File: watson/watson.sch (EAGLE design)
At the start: 37 parts

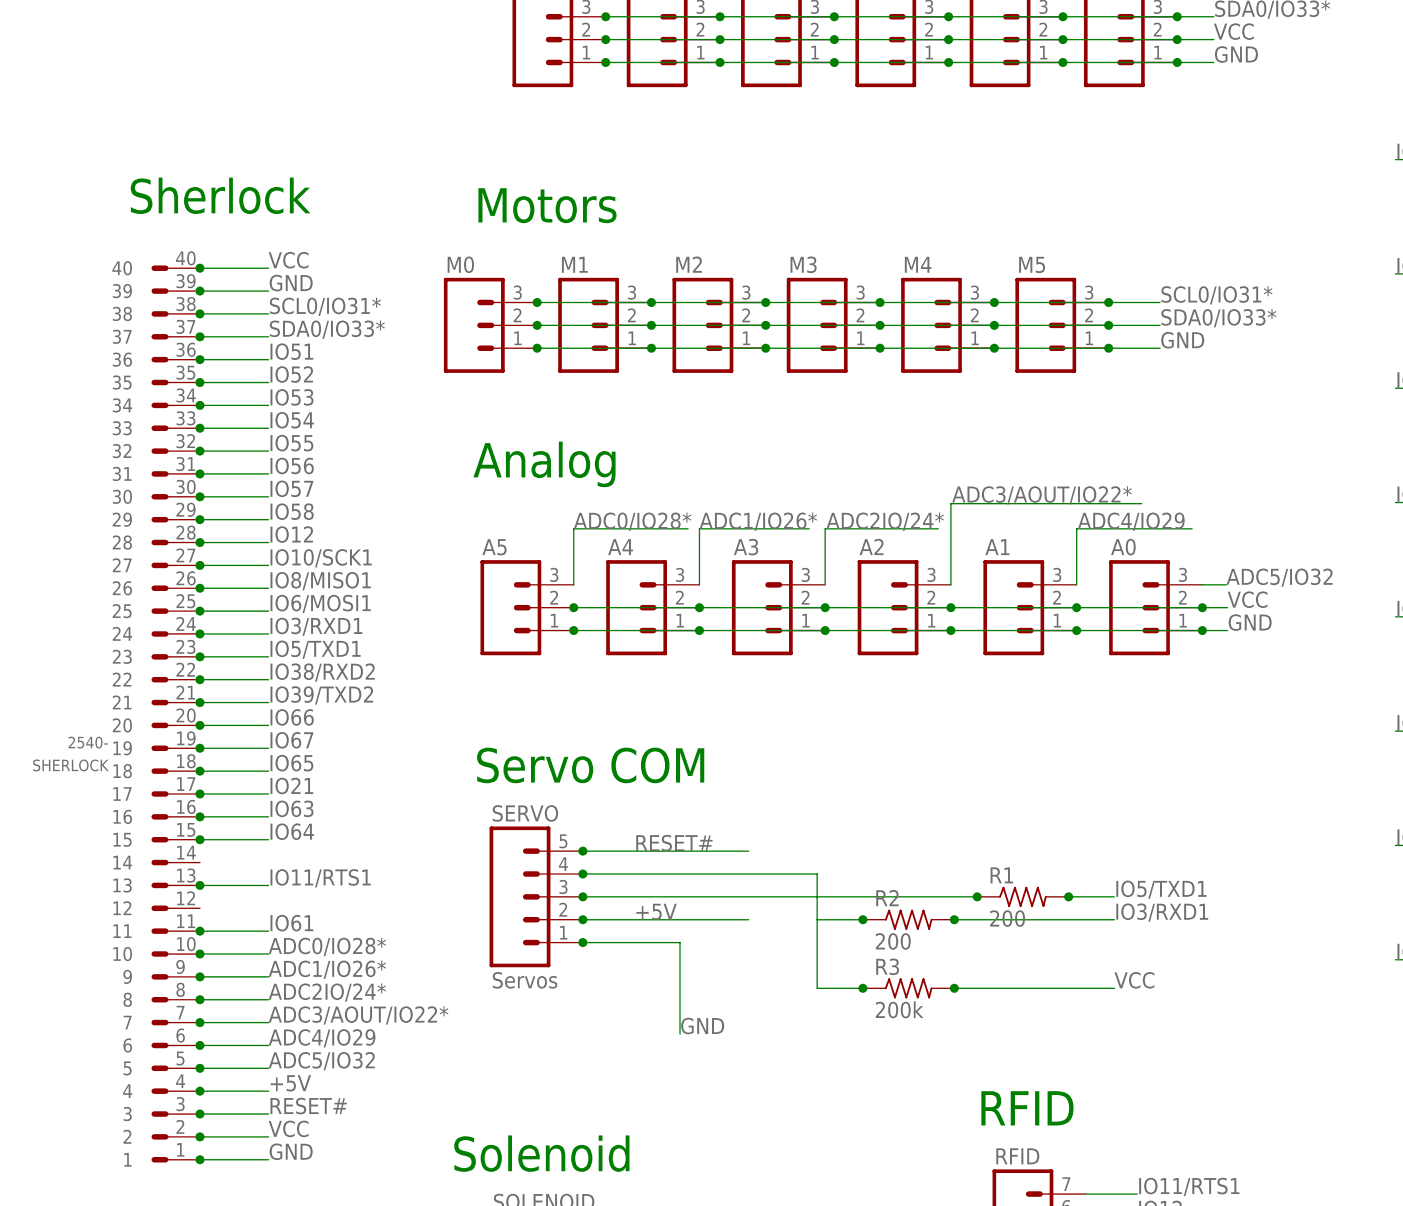
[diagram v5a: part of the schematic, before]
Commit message: Sherlock/Watson/Solenoid Rev E (Again)
Had to make a few simple changes Dennis requested.
This is the final version. Rev F will only contain
extra copyright material.

Sherlcok DFM: https://www.freedfm.com/freedfm/0019486703424644/results/summary2.htm
Watson DFM: https://www.freedfm.com/freedfm/0019486703424641/results/summary2.htm
Solenoid DFM: https://www.freedfm.com/freedfm/0019486703424640/results/summary2.htm

Change-Id: Ibaa3e17f4a8e9033ce9bcff25cf747d321aea476
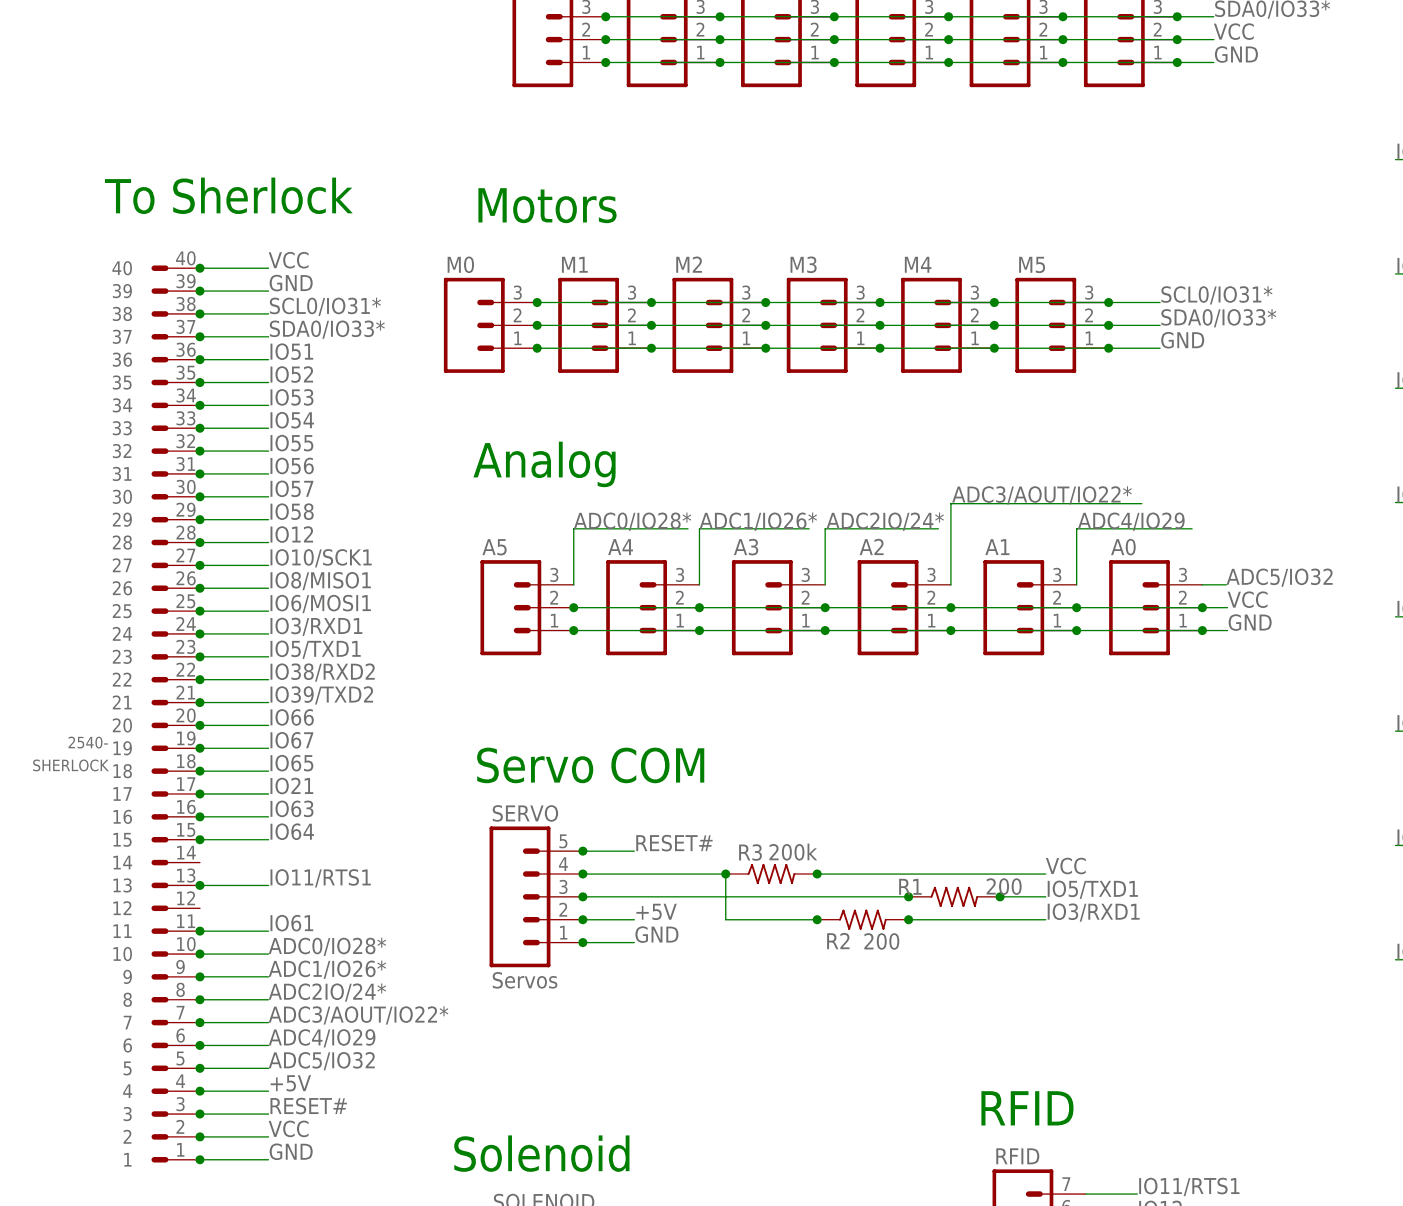
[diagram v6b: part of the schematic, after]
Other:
- note added: "To Sherlock"
- note removed: "Sherlock"
- moved on the sheet: R1, R2, R3
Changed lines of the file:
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@@
 <setting verticaltext="up"/>
 </settings>
-<grid distance="0.005" unitdist="inch" unit="inch" style="lines" multiple="1" display="no" altdistance="0.01" altunitdist="inch" altunit="inch"/>
+<grid distance="0.05" unitdist="inch" unit="inch" style="lines" multiple="1" display="no" altdistance="0.01" altunitdist="inch" altunit="inch"/>
 <layers>
 <layer number="1" name="Top" color="4" fill="1" visible="no" active="no"/>
@@
 <text x="193.04" y="71.12" size="3.81" layer="91">SIMPLE Extension</text>
 <text x="50.8" y="35.56" size="3.81" layer="91">Solenoid</text>
-<text x="14.859" y="141.986" size="3.81" layer="91">Sherlock</text>
+<text x="12.319" y="141.986" size="3.81" layer="91">To Sherlock</text>
 </plain>
 <instances>
@@
 <instance part="I2C0" gate="G$1" x="60.96" y="162.56"/>
 <instance part="RFID" gate="G$1" x="114.3" y="25.4"/>
-<instance part="R1" gate="G$1" x="114.3" y="66.04"/>
-<instance part="R2" gate="G$1" x="101.6" y="63.5"/>
-<instance part="R3" gate="G$1" x="101.6" y="55.88"/>
+<instance part="R1" gate="G$1" x="106.68" y="66.04" smashed="yes">
+<attribute name="NAME" x="100.33" y="66.2686" size="1.778" layer="95"/>
+<attribute name="VALUE" x="114.3" y="68.072" size="1.778" layer="96" rot="R180"/>
+</instance>
+<instance part="R2" gate="G$1" x="96.52" y="63.5" smashed="yes">
+<attribute name="NAME" x="95.25" y="62.0014" size="1.778" layer="95" rot="R180"/>
+<attribute name="VALUE" x="96.52" y="60.198" size="1.778" layer="96"/>
+</instance>
+<instance part="R3" gate="G$1" x="86.36" y="68.58" smashed="yes">
+<attribute name="NAME" x="82.55" y="70.0786" size="1.778" layer="95"/>
+<attribute name="VALUE" x="91.44" y="71.882" size="1.778" layer="96" rot="R180"/>
+</instance>
 <instance part="SIMPLE" gate="G$1" x="190.5" y="58.42"/>
 <instance part="SOLENOID" gate="G$1" x="58.547" y="21.59"/>
@@
 <segment>
 <pinref part="SERVO" gate="G$1" pin="1"/>
-<wire x1="65.405" y1="60.96" x2="76.2" y2="60.96" width="0.1524" layer="91"/>
-<wire x1="76.2" y1="60.96" x2="76.2" y2="50.8" width="0.1524" layer="91"/>
+<wire x1="65.405" y1="60.96" x2="71.12" y2="60.96" width="0.1524" layer="91"/>
 <junction x="65.405" y="60.96"/>
-<label x="76.2" y="50.8" size="1.778" layer="95"/>
+<label x="71.12" y="60.96" size="1.778" layer="95"/>
 </segment>
 <segment>
@@
 <segment>
 <pinref part="R3" gate="G$1" pin="2"/>
-<junction x="106.68" y="55.88"/>
-<wire x1="106.68" y1="55.88" x2="124.46" y2="55.88" width="0.1524" layer="91"/>
-<label x="124.46" y="55.88" size="1.778" layer="95"/>
+<junction x="91.44" y="68.58"/>
+<wire x1="91.44" y1="68.58" x2="116.84" y2="68.58" width="0.1524" layer="91"/>
+<label x="116.84" y="68.58" size="1.778" layer="95"/>
 </segment>
 <segment>
@@
 <pinref part="SERVO" gate="G$1" pin="5"/>
 <junction x="65.405" y="71.12"/>
-<wire x1="65.405" y1="71.12" x2="83.82" y2="71.12" width="0.1524" layer="91"/>
+<wire x1="65.405" y1="71.12" x2="71.12" y2="71.12" width="0.1524" layer="91"/>
 <label x="71.12" y="71.12" size="1.778" layer="95"/>
 </segment>
@@
 <segment>
 <pinref part="R2" gate="G$1" pin="2"/>
-<junction x="106.68" y="63.5"/>
-<wire x1="106.68" y1="63.5" x2="124.46" y2="63.5" width="0.1524" layer="91"/>
-<label x="124.46" y="63.5" size="1.778" layer="95"/>
+<junction x="101.6" y="63.5"/>
+<wire x1="101.6" y1="63.5" x2="116.84" y2="63.5" width="0.1524" layer="91"/>
+<label x="116.84" y="63.5" size="1.778" layer="95"/>
 </segment>
 </net>
@@
 <segment>
 <pinref part="SERVO" gate="G$1" pin="2"/>
-<wire x1="65.405" y1="63.5" x2="83.82" y2="63.5" width="0.1524" layer="91"/>
+<wire x1="65.405" y1="63.5" x2="71.12" y2="63.5" width="0.1524" layer="91"/>
 <junction x="65.405" y="63.5"/>
 <label x="71.12" y="63.5" size="1.778" layer="95"/>
@@
 <segment>
 <pinref part="R2" gate="G$1" pin="1"/>
-<wire x1="91.44" y1="63.5" x2="96.52" y2="63.5" width="0.1524" layer="91"/>
-<wire x1="91.44" y1="63.5" x2="91.44" y2="55.88" width="0.1524" layer="91"/>
+<wire x1="81.28" y1="63.5" x2="91.44" y2="63.5" width="0.1524" layer="91"/>
 <pinref part="R3" gate="G$1" pin="1"/>
-<wire x1="91.44" y1="55.88" x2="96.52" y2="55.88" width="0.1524" layer="91"/>
-<junction x="96.52" y="55.88"/>
-<junction x="96.52" y="63.5"/>
+<junction x="81.28" y="68.58"/>
+<junction x="91.44" y="63.5"/>
 <pinref part="SERVO" gate="G$1" pin="4"/>
-<wire x1="65.405" y1="68.58" x2="91.44" y2="68.58" width="0.1524" layer="91"/>
-<wire x1="91.44" y1="68.58" x2="91.44" y2="63.5" width="0.1524" layer="91"/>
+<wire x1="65.405" y1="68.58" x2="81.28" y2="68.58" width="0.1524" layer="91"/>
+<wire x1="81.28" y1="68.58" x2="81.28" y2="63.5" width="0.1524" layer="91"/>
 <junction x="65.405" y="68.58"/>
 </segment>
@@
 <pinref part="SERVO" gate="G$1" pin="3"/>
 <pinref part="R1" gate="G$1" pin="1"/>
-<wire x1="65.405" y1="66.04" x2="109.22" y2="66.04" width="0.1524" layer="91"/>
-<junction x="109.22" y="66.04"/>
+<wire x1="65.405" y1="66.04" x2="101.6" y2="66.04" width="0.1524" layer="91"/>
+<junction x="101.6" y="66.04"/>
 <junction x="65.405" y="66.04"/>
 </segment>
@@
 <segment>
 <pinref part="R1" gate="G$1" pin="2"/>
-<junction x="119.38" y="66.04"/>
-<wire x1="119.38" y1="66.04" x2="124.46" y2="66.04" width="0.1524" layer="91"/>
-<label x="124.46" y="66.04" size="1.778" layer="95"/>
-</segment>
-</net>
+<junction x="111.76" y="66.04"/>
+<wire x1="111.76" y1="66.04" x2="116.84" y2="66.04" width="0.1524" layer="91"/>
+<label x="116.84" y="66.04" size="1.778" layer="95"/>
+</segment>
+</net>

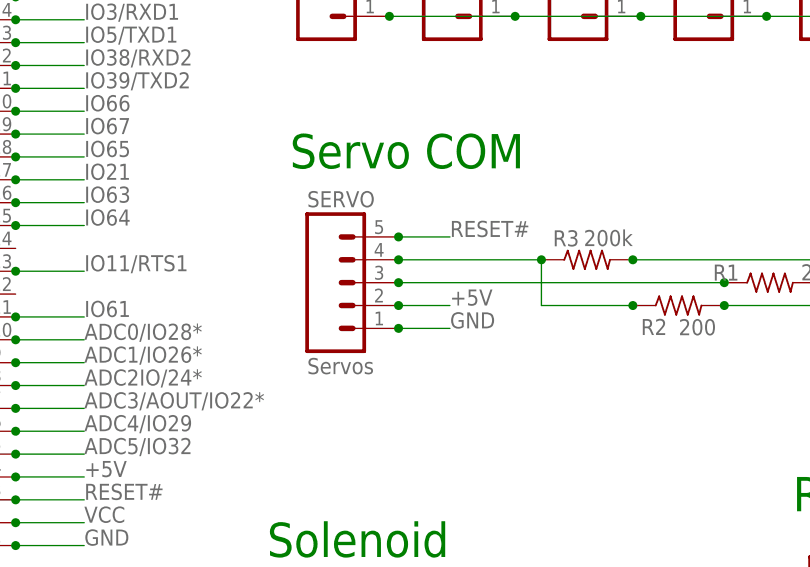
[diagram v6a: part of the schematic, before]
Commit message: Sherlock, Watson, Solenoid Rev F
- Removed 5V pin from Servo on Watson
- Removed Low Battery LED on Sherlock
- Added copyright info to all boards
- Put OSHW logos in pie.lbr

Sherlock DFM: https://www.freedfm.com/freedfm/0019486703437089/results/summary2.htm
Watson DFM: https://www.freedfm.com/freedfm/0019486703437092/results/summary2.htm
Solenoid DFM: https://www.freedfm.com/freedfm/0019486703437091/results/summary2.htm

Change-Id: I06acc4df022cd5501e47e2ba488eae3a4c23d9a5
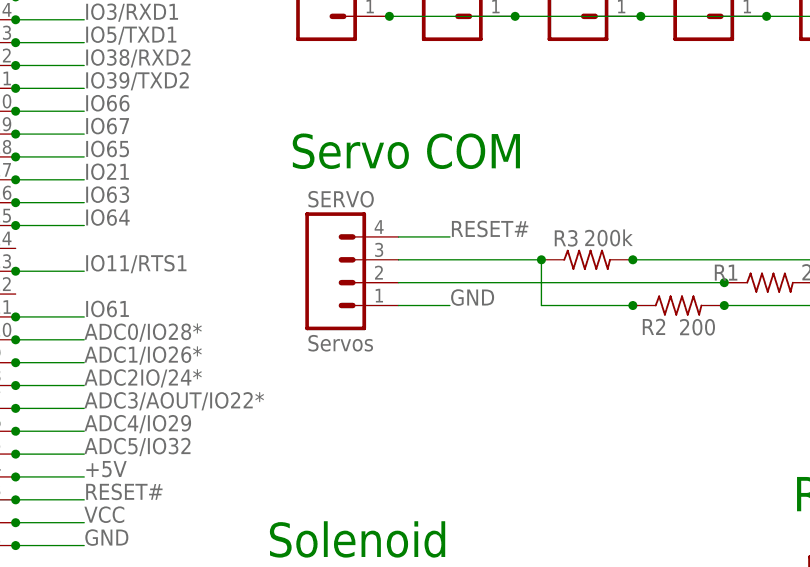
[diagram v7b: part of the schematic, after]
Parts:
- SERVO: device pie:M05MTA -> pie:M041X04-MTA
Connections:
- net +5V: no longer SERVO.2
- net N$1: now also SERVO.3; no longer SERVO.4
- net N$2: now also SERVO.2; no longer SERVO.3
- net RESET#: now also SERVO.4; no longer SERVO.5
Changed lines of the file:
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@@
 <part name="M5" library="pie" deviceset="M03" device="1X03-MTA"/>
 <part name="FLAG" library="pie" deviceset="M03" device="1X03-MTA"/>
-<part name="SERVO" library="pie" deviceset="M05" device="MTA" value="Servos"/>
 <part name="I2C5" library="pie" deviceset="M04" device="1X04-MTA"/>
 <part name="I2C4" library="pie" deviceset="M04" device="1X04-MTA"/>
@@
 <part name="FRAME1" library="pie" deviceset="FRAME-LETTER" device="">
 <attribute name="AUTHOR" value="Michael C., Sumita G., Sahar M."/>
-<attribute name="REVISION" value="E"/>
+<attribute name="REVISION" value="F"/>
 </part>
 <part name="SHERLOCK" library="pie" deviceset="2540-" device=""/>
+<part name="SERVO" library="pie" deviceset="M04" device="1X04-MTA" value="Servos"/>
 </parts>
 <sheets>
@@
 <instance part="M5" gate="G$1" x="116.84" y="129.54"/>
 <instance part="FLAG" gate="G$1" x="198.12" y="91.44"/>
-<instance part="SERVO" gate="G$1" x="58.42" y="66.04"/>
 <instance part="I2C5" gate="G$1" x="124.46" y="162.56"/>
 <instance part="I2C4" gate="G$1" x="111.76" y="162.56"/>
@@
 </instance>
 <instance part="SHERLOCK" gate="G$1" x="17.78" y="86.36" rot="R180"/>
+<instance part="SERVO" gate="G$1" x="58.42" y="67.31"/>
 </instances>
 <busses>
@@
 </segment>
 <segment>
+<wire x1="65.405" y1="63.5" x2="71.12" y2="63.5" width="0.1524" layer="91"/>
+<label x="71.12" y="63.5" size="1.778" layer="95"/>
 <pinref part="SERVO" gate="G$1" pin="1"/>
-<wire x1="65.405" y1="60.96" x2="71.12" y2="60.96" width="0.1524" layer="91"/>
-<junction x="65.405" y="60.96"/>
-<label x="71.12" y="60.96" size="1.778" layer="95"/>
 </segment>
 <segment>
@@
 </segment>
 <segment>
-<pinref part="SERVO" gate="G$1" pin="5"/>
-<junction x="65.405" y="71.12"/>
 <wire x1="65.405" y1="71.12" x2="71.12" y2="71.12" width="0.1524" layer="91"/>
 <label x="71.12" y="71.12" size="1.778" layer="95"/>
+<pinref part="SERVO" gate="G$1" pin="4"/>
 </segment>
 </net>
@@
 <pinref part="SHERLOCK" gate="G$1" pin="4"/>
 <junction x="22.86" y="44.45"/>
-</segment>
-<segment>
-<pinref part="SERVO" gate="G$1" pin="2"/>
-<wire x1="65.405" y1="63.5" x2="71.12" y2="63.5" width="0.1524" layer="91"/>
-<junction x="65.405" y="63.5"/>
-<label x="71.12" y="63.5" size="1.778" layer="95"/>
 </segment>
 <segment>
@@
 <junction x="81.28" y="68.58"/>
 <junction x="91.44" y="63.5"/>
-<pinref part="SERVO" gate="G$1" pin="4"/>
 <wire x1="65.405" y1="68.58" x2="81.28" y2="68.58" width="0.1524" layer="91"/>
 <wire x1="81.28" y1="68.58" x2="81.28" y2="63.5" width="0.1524" layer="91"/>
-<junction x="65.405" y="68.58"/>
+<pinref part="SERVO" gate="G$1" pin="3"/>
 </segment>
 </net>
 <net name="N$2" class="0">
 <segment>
-<pinref part="SERVO" gate="G$1" pin="3"/>
 <pinref part="R1" gate="G$1" pin="1"/>
 <wire x1="65.405" y1="66.04" x2="101.6" y2="66.04" width="0.1524" layer="91"/>
 <junction x="101.6" y="66.04"/>
-<junction x="65.405" y="66.04"/>
-</segment>
-</net>
+<pinref part="SERVO" gate="G$1" pin="2"/>
+</segment>
+</net>
